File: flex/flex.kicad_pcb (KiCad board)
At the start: 2 copper layers, 126.3 x 113 mm, 105 parts, among them J1 Conn_01x06_Female, J2 Conn_01x05_Female, J3 Conn_01x03_Female, J4 Conn_01x06_Female, J5 Conn_01x03_Female, SW1 SW_Push, SW10 SW_Push, SW11 SW_Push, SW12 SW_Push, SW14 SW_Push, SW15 SW_Push, SW16 SW_Push, SW17 SW_Push, SW19 SW_Push, SW2 SW_Push, SW20 SW_Push, SW21 SW_Push, SW22 SW_Push, SW23 SW_Push, SW24 SW_Push, SW25 SW_Push, SW26 SW_Push, SW3 SW_Push, SW4 SW_Push, SW5 SW_Push, SW6 SW_Push, SW7 SW_Push, SW8 SW_Push, SW9 SW_Push

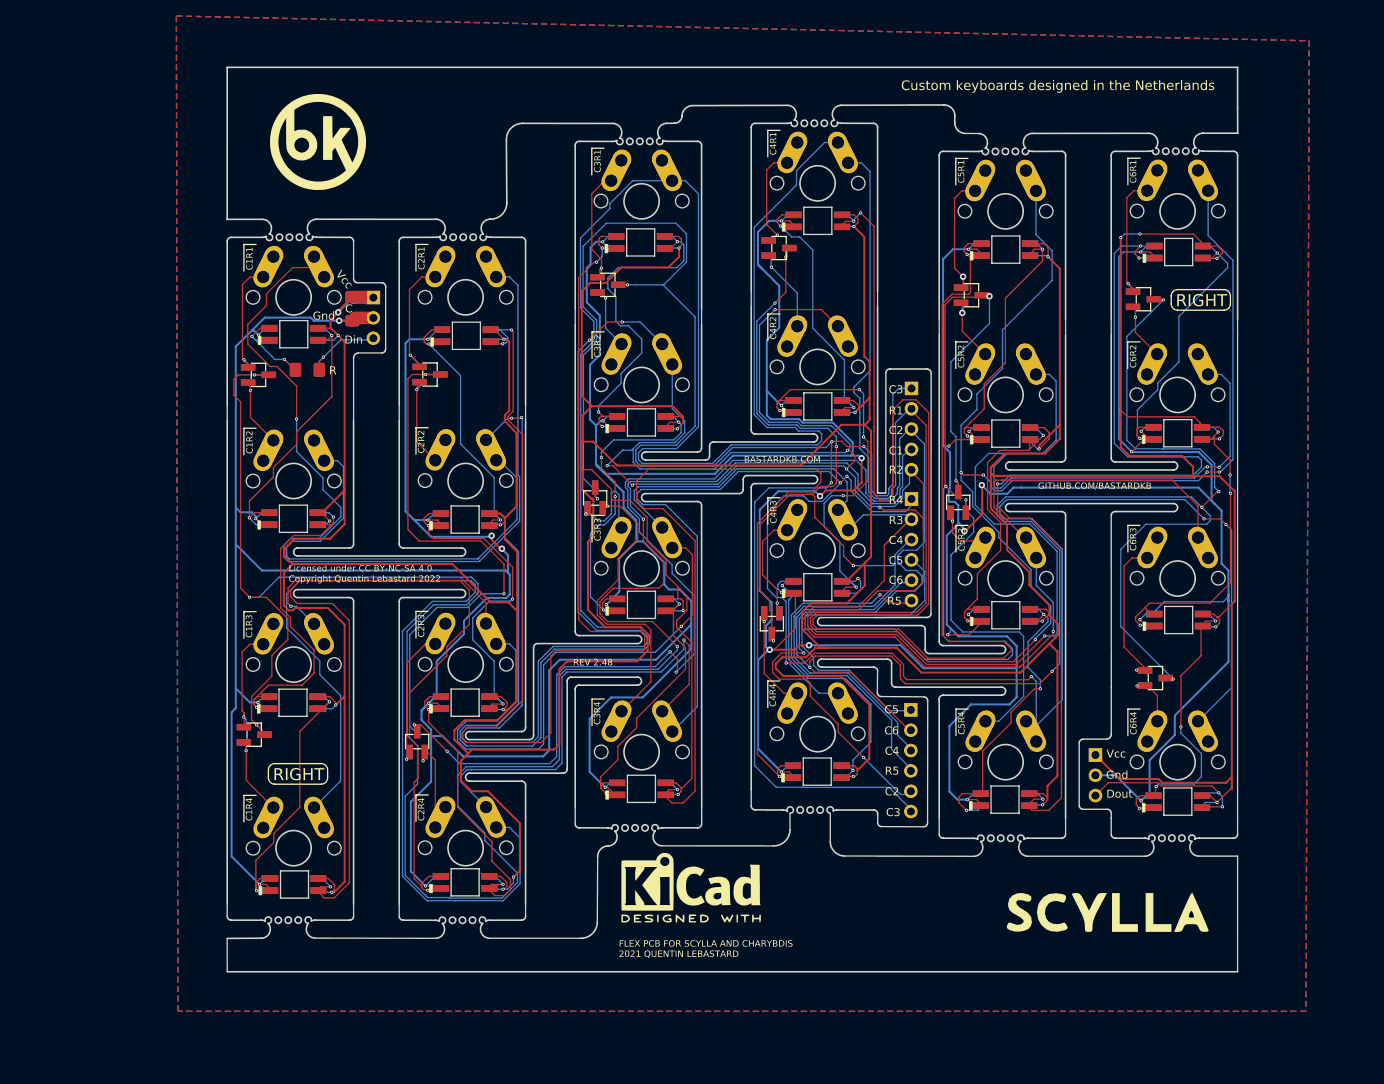
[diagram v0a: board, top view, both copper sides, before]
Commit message: added hotswap footprint
currently incomplete, imported daprice's Kailh footprint and modified it to fit flip it horizontally.
Will continue some other time.
Major kudos to bastardkb for already making the pcb flippable!
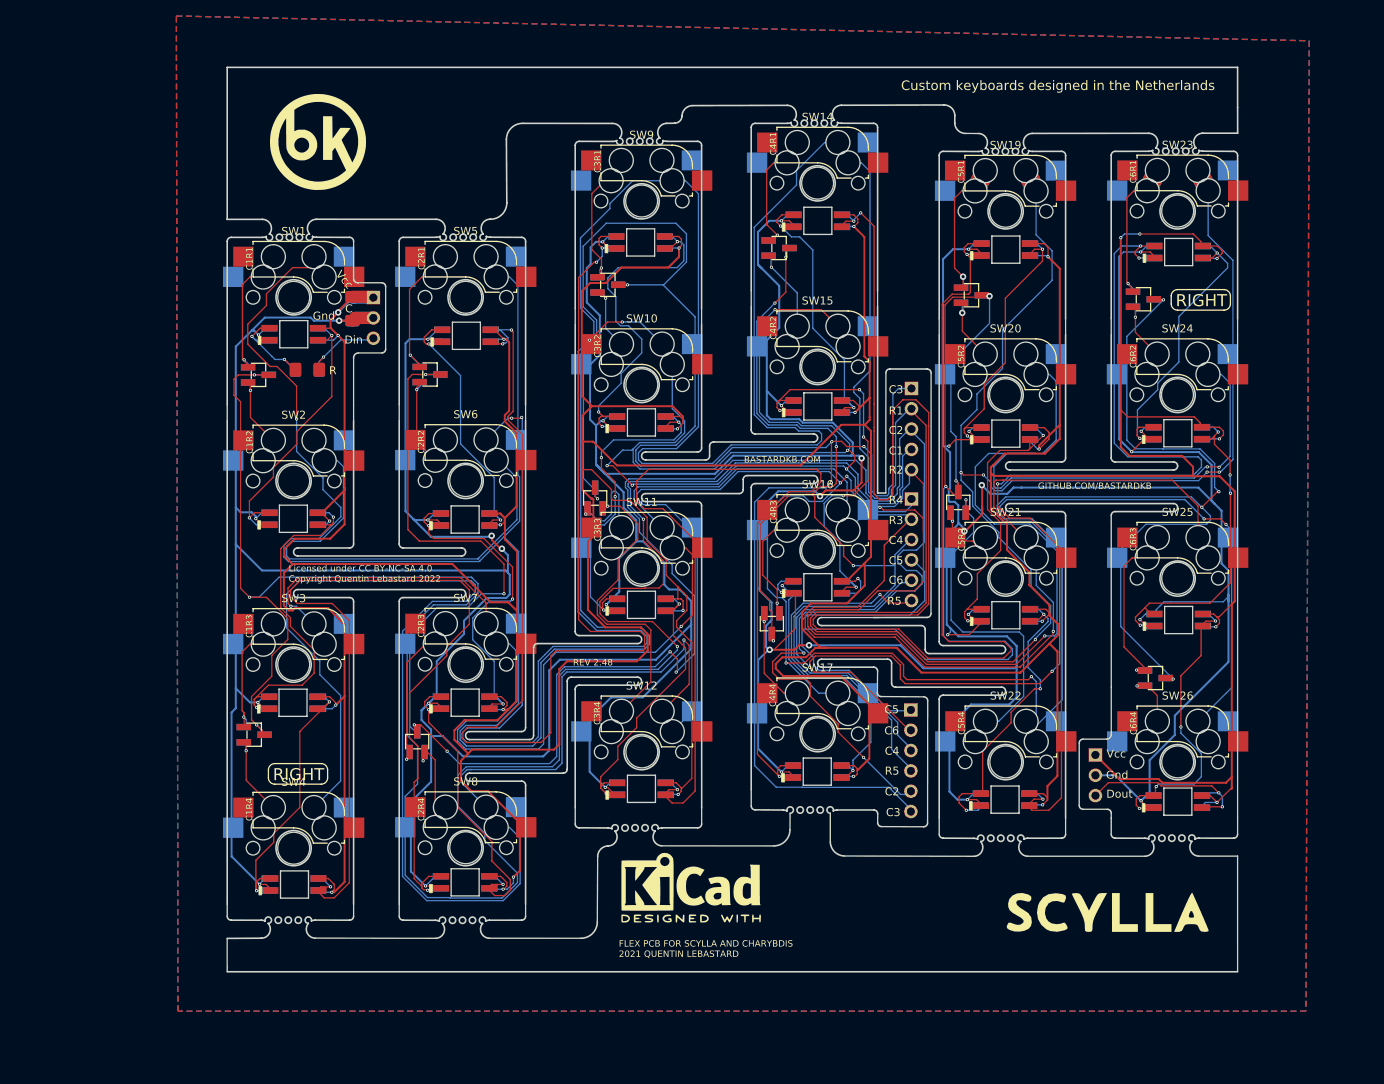
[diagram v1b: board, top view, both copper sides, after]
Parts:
- removed the G*** at (366.7, 111.2)
- removed the G*** at (277.7, 122.3)
- removed the G*** at (278.1, 122.6)
- removed the G*** at (366.4, 111.2)
- removed the G*** at (266.9, 142.5)
- removed the G*** at (267.0, 148.6)
- SW1, SW10, SW11, SW12, SW14, SW15, SW16, SW17, SW19, SW2, SW20, SW21, SW22, SW23, SW24, SW25, SW26, SW3, SW4, SW5, SW6, SW7, SW8, SW9: footprint custom:SW_MX_reversible -> Kailh_sockets:Kailh_socket_MX_flippable
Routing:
- net Vcc: track 926.6 -> 5253.8 mm, vias 28 -> 146
- net Gnd: track 897.9 -> 0.00 mm, vias 36 -> 0
- net row2: track 513.7 -> 58.9 mm, vias 13 -> 0
- net row1: track 655.7 -> 282.5 mm, vias 6 -> 5
- net row4: track 431.2 -> 58.3 mm, vias 7 -> 1
- net col1: track 286.0 -> 0.00 mm, vias 5 -> 0
- net col2: track 273.8 -> 0.00 mm, vias 8 -> 0
- net col3: track 218.7 -> 0.00 mm, vias 5 -> 0
- net col6: track 204.1 -> 0.00 mm, vias 6 -> 0
- net Net-(D19-Pad3): track 164.0 -> 0.00 mm, vias 4 -> 0
- net col5: track 160.7 -> 0.00 mm, vias 3 -> 0
- net row3: track 262.8 -> 113.5 mm, vias 3 -> 1
- net col4: track 131.7 -> 0.00 mm, vias 5 -> 0
- net Net-(D51-Pad1): track 126.2 -> 0.00 mm, vias 4 -> 0
- net Net-(D25-Pad1): track 125.7 -> 0.00 mm, vias 2 -> 0
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
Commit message: fixed outline, started routing
Softly confused bout the doubled diode footprint. Assume that they are for flexibility. Will probably do something about it.
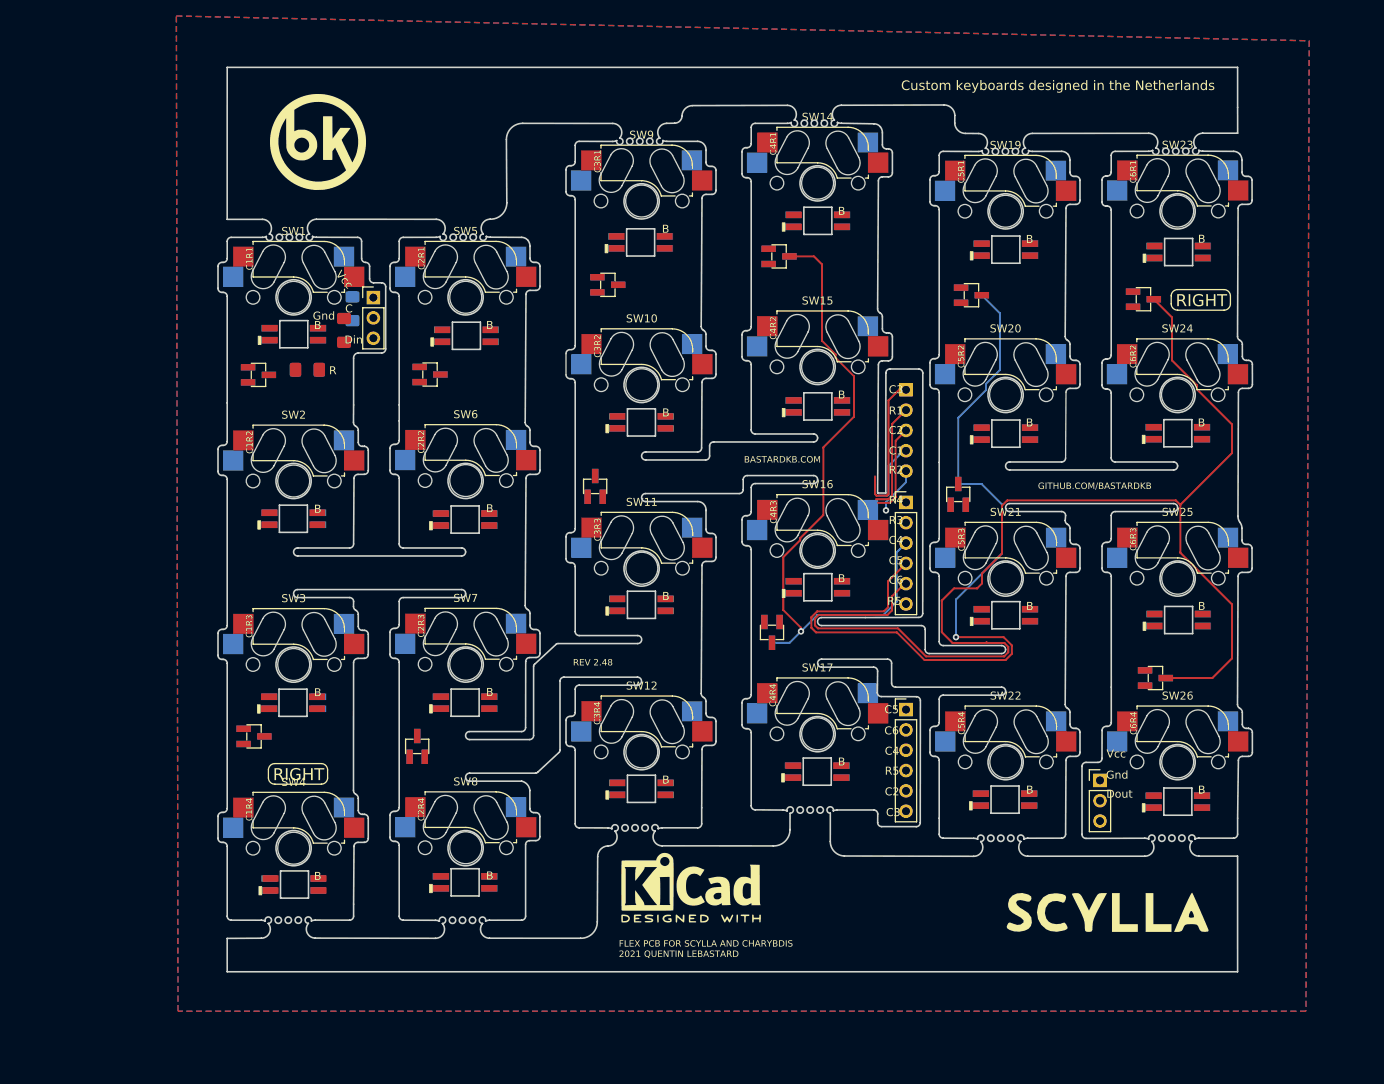
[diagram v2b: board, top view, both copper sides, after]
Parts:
- moved J5 3.23 mm to (144.5, 115.7)
- moved C1 2.91 mm to (50.0, 59.5), turned to 90 degrees
- moved D10 1.45 mm to (81.4, 79.0)
- moved D12 1.10 mm to (103.5, 97.2)
- moved D11 1.05 mm to (104.4, 50.2)
- moved D15 1.00 mm to (126.8, 80.0)
- moved J4 0.81 mm to (120.3, 81.0)
- moved J2 0.71 mm to (120.3, 66.9)
- moved J1 0.61 mm to (120.3, 106.9)
- moved D32 0.60 mm to (59.2, 111.5)
- moved D1 0.22 mm to (38.8, 110.2)
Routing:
- net Vcc: track 5253.8 -> 0.00 mm, vias 146 -> 0
- net row1: track 282.5 -> 13.6 mm, vias 5 -> 0
- net Net-(D43-Pad1): track 192.7 -> 0.00 mm, vias 3 -> 0
- net col6: track 0.00 -> 158.2 mm
- net row3: track 113.5 -> 0.00 mm, vias 1 -> 0
- net col5: track 0.00 -> 105.5 mm, vias 0 -> 1
- net col4: track 0.00 -> 82.1 mm, vias 0 -> 1
- net row4: track 58.3 -> 0.00 mm, vias 1 -> 0
- net Net-(D5-Pad1): track 53.1 -> 0.00 mm, vias 3 -> 0
- net row2: track 58.9 -> 5.95 mm, vias 0 -> 1
- net Net-(D39-Pad1): track 51.8 -> 0.00 mm, vias 5 -> 0
- net Net-(D19-Pad1): track 47.7 -> 0.00 mm, vias 3 -> 0
- net Net-(D18-Pad3): track 47.1 -> 0.00 mm, vias 3 -> 0
- net Net-(D2-Pad1): track 47.1 -> 0.00 mm, vias 3 -> 0
- net Net-(D33-Pad3): track 45.6 -> 0.00 mm, vias 3 -> 0
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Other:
- board size 126.3 x 113 mm -> 129.3 x 113 mm
- board text removed: "Licensed under CC BY-NC-SA 4.0 Copyright Quentin Lebastard 2022"

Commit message: Wired most of it
Diodes and cleanup left
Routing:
- net row1: track 13.6 -> 586.8 mm, vias 0 -> 13
- net row4: track 0.00 -> 432.2 mm, vias 0 -> 23
- net row2: track 5.95 -> 423.1 mm, vias 1 -> 20
- net row3: track 0.00 -> 322.0 mm, vias 0 -> 14
- net Net-(D43-Pad1): track 0.00 -> 178.9 mm, vias 0 -> 19
- net Net-(D19-Pad3): track 0.00 -> 166.9 mm, vias 0 -> 9
- net Net-(D18-Pad1): track 0.00 -> 130.0 mm, vias 0 -> 7
- net Net-(D25-Pad1): track 0.00 -> 126.9 mm, vias 0 -> 9
- net Net-(D51-Pad1): track 0.00 -> 125.2 mm, vias 0 -> 9
- net col3: track 18.5 -> 82.6 mm, vias 0 -> 8
- net Net-(D21-Pad1): track 0.00 -> 53.6 mm, vias 0 -> 5
- net Net-(D57-Pad1): track 0.00 -> 43.6 mm, vias 0 -> 2
- net Vcc: track 0.00 -> 40.8 mm, vias 0 -> 22
- net Net-(D37-Pad1): track 0.00 -> 40.6 mm, vias 0 -> 5
- net Net-(D47-Pad1): track 0.00 -> 40.5 mm, vias 0 -> 6
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- added copper zone on B.Cu, net Vcc
- removed copper zone on B.Cu, net Gnd
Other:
- outline, holes or cut-outs redrawn

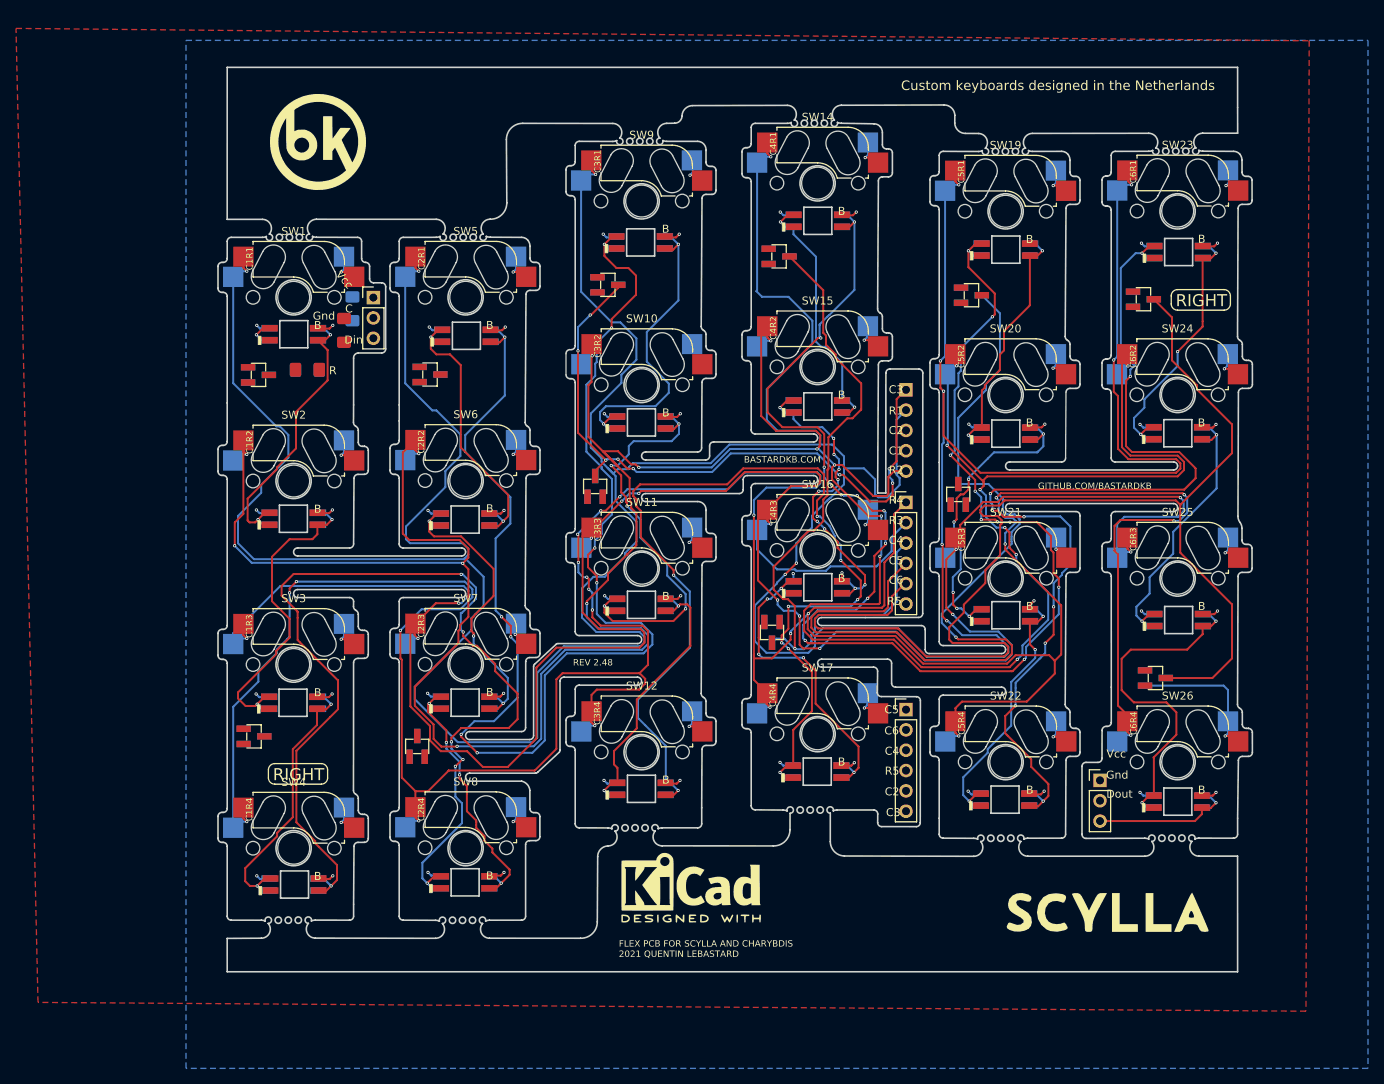
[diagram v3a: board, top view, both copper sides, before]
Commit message: Routed diodes
now only the planes need to connect
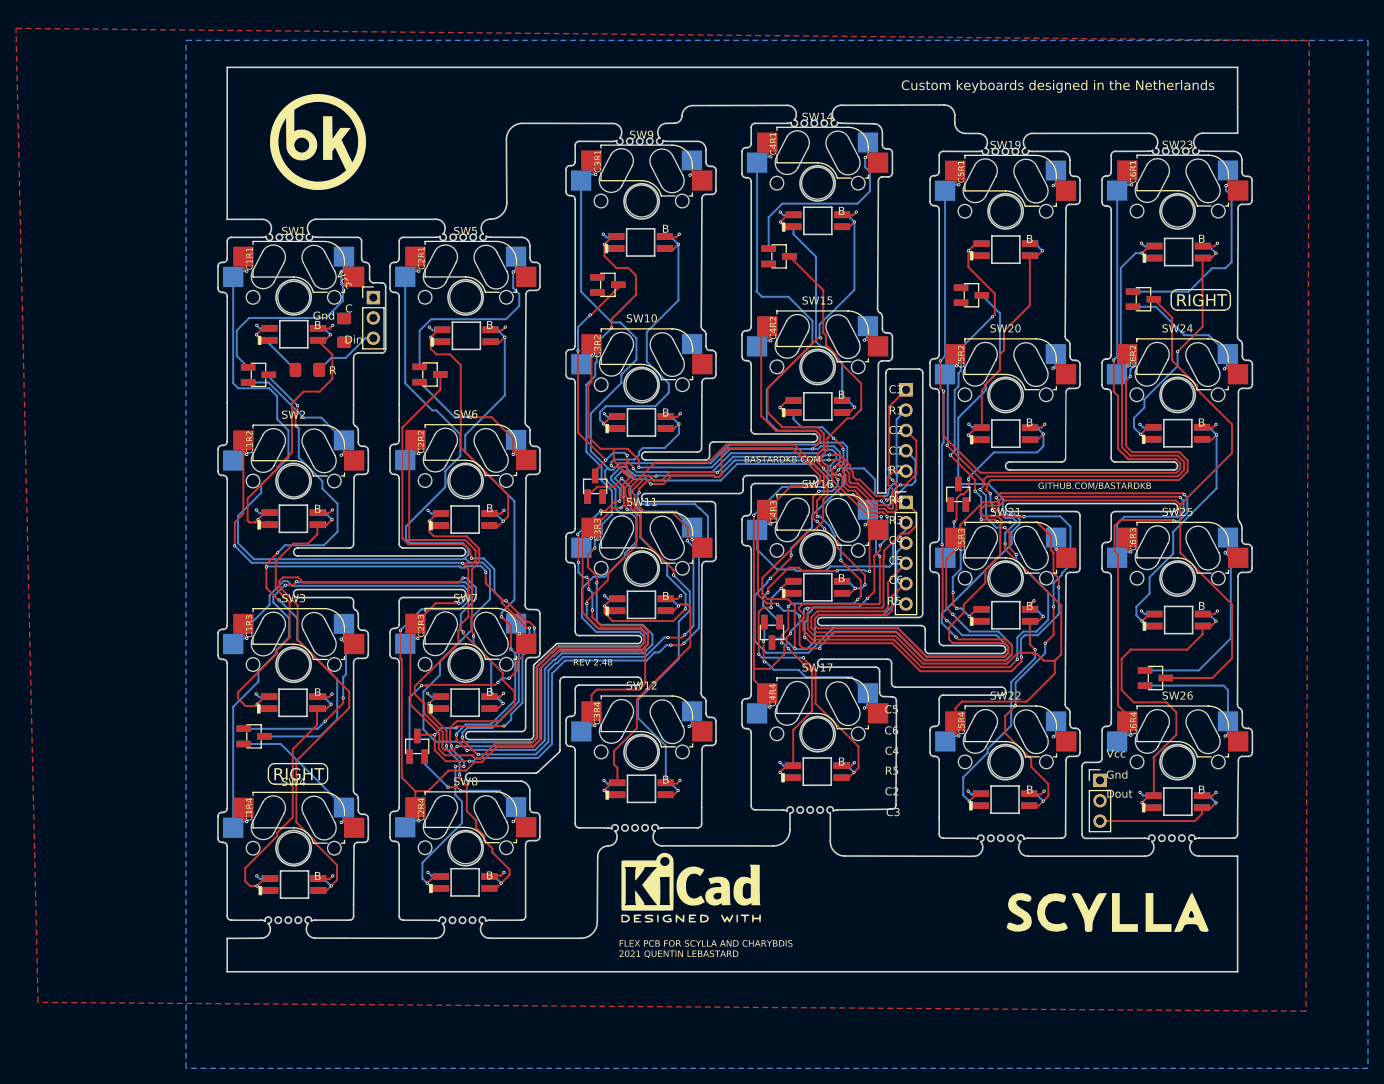
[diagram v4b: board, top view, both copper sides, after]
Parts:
- removed J1: Conn_01x06_Female, Connector_PinHeader_2.54mm:PinHeader_1x06_P2.54mm_Vertical
- moved C2 2.90 mm to (50.0, 59.5), turned to 90 degrees
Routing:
- net col1: track 0.00 -> 233.7 mm, vias 0 -> 15
- net col2: track 0.00 -> 191.4 mm, vias 0 -> 14
- net Net-(D32-Pad2): track 3.05 -> 29.1 mm, vias 1 -> 4
- net Net-(D12-Pad2): track 3.89 -> 28.9 mm, vias 1 -> 4
- net Net-(D16-Pad2): track 3.89 -> 27.6 mm
- net Net-(D13-Pad2): track 3.89 -> 27.6 mm
- net Net-(D17-Pad2): track 3.89 -> 27.3 mm
- net Net-(D31-Pad2): track 3.89 -> 26.7 mm
- net Net-(D11-Pad2): track 3.89 -> 26.3 mm
- net Net-(D1-Pad2): track 3.89 -> 26.1 mm, vias 1 -> 3
- net Net-(D12-Pad1): track 3.89 -> 23.5 mm, vias 1 -> 3
- net Net-(D10-Pad2): track 3.89 -> 20.8 mm, vias 1 -> 2
- net Net-(D31-Pad1): track 3.89 -> 20.5 mm, vias 1 -> 2
- net row4: track 432.2 -> 448.6 mm
- net Net-(D1-Pad1): track 3.89 -> 19.8 mm
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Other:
- outline, holes or cut-outs redrawn
